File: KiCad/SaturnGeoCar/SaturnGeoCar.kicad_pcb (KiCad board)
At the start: 2 copper layers, 1 part, among them U3 ESP32-WROVER-E

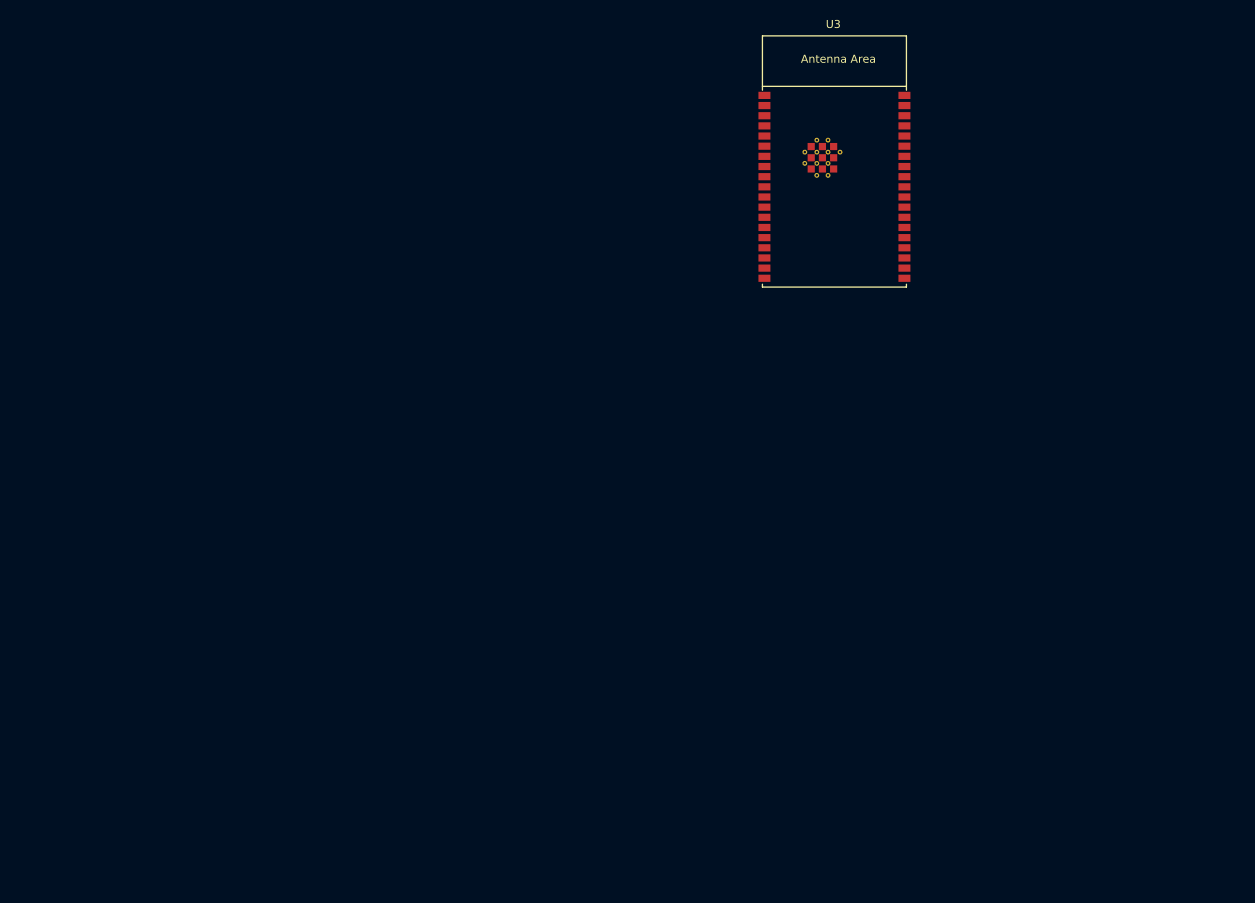
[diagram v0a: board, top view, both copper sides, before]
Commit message: Finished uploading all components, wiring has started
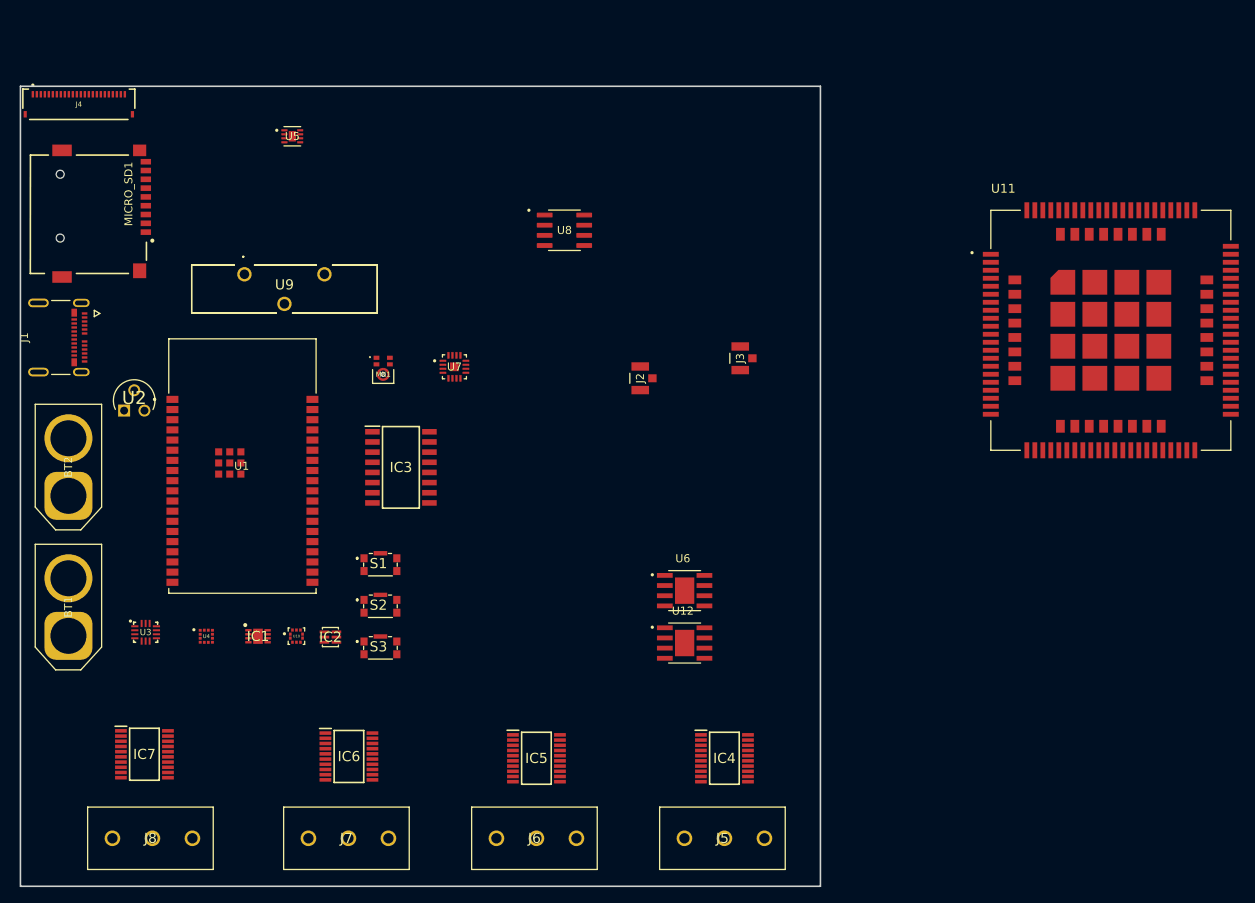
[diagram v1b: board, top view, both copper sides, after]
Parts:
- added BT1: XT60-F, Connector_AMASS:AMASS_XT60-F_1x02_P7.20mm_Vertical, F.Cu at (69.0, 139.7)
- added BT2: XT60-F, Connector_AMASS:AMASS_XT60-F_1x02_P7.20mm_Vertical, F.Cu at (69.0, 122.2)
- added IC1: SHT30-ARP-B2.5KS, SHT30-ARP-B2.5KS:SON50P250X250X100-9N-D, F.Cu at (92.7, 139.8)
- added IC2: TSL25911FN, TSL25911FN:TSL25911FN, F.Cu at (101.8, 139.8)
- added IC3: SN74HC165NSR, SN74HC165NSR:SOIC127P780X200-16N, F.Cu at (110.6, 118.6)
- added IC4: DRV8300DPWR, DRV8300DPWR:SOP65P640X120-20N, F.Cu at (151.0, 155.0)
- added IC5: DRV8300DPWR, DRV8300DPWR:SOP65P640X120-20N, F.Cu at (127.5, 155.0)
- added IC6: DRV8300DPWR, DRV8300DPWR:SOP65P640X120-20N, F.Cu at (104.1, 154.8)
- added IC7: DRV8300DPWR, DRV8300DPWR:SOP65P640X120-20N, F.Cu at (78.5, 154.5)
- added J1: 1054500101, FilesNeeded:MOLEX_1054500101, F.Cu at (63.5, 102.4)
- added J2: U.FL-R-SMT-1_80_, U.FL-R-SMT-1_80_:HIROSE_U.FL-R-SMT-1_80_, F.Cu at (140.5, 107.5)
- added J3: U.FL-R-SMT-1_80_, U.FL-R-SMT-1_80_:HIROSE_U.FL-R-SMT-1_80_, F.Cu at (153.0, 105.0)
- added J4: FFC2B28-24-G, FFC2B28-24-G:GCT_FFC2B28-24-G, F.Cu at (70.3, 73.2)
- added J5: WJ126V-5.0-3P, WJ126V-5.0-3P:WJ126V503P, F.Cu at (146.0, 165.0)
- added J6: WJ126V-5.0-3P, WJ126V-5.0-3P:WJ126V503P, F.Cu at (122.5, 165.0)
- added J7: WJ126V-5.0-3P, WJ126V-5.0-3P:WJ126V503P, F.Cu at (99.0, 165.0)
- added J8: WJ126V-5.0-3P, WJ126V-5.0-3P:WJ126V503P, F.Cu at (74.5, 165.0)
- added MICRO_SD1: TF-01A, TF-01A:TF-01A, F.Cu at (71.5, 87.0)
- added MK1: SPH0641LU4H-1, SPH0641LU4H-1:MIC_SPH0641LU4H-1, F.Cu at (108.3, 107.0)
- added S1: KMR221GLFS, KMR221GLFS:KMR231GLFS, F.Cu at (108.0, 130.8)
- added S2: KMR221GLFS, KMR221GLFS:KMR231GLFS, F.Cu at (108.0, 136.0)
- added S3: KMR221GLFS, KMR221GLFS:KMR231GLFS, F.Cu at (108.0, 141.2)
- added U1: ESP32-WROVER-E-N16R8, footprints:ESP32-WROVER-E_EXP, F.Cu at (90.8, 118.5)
- added U10: BMP388, BMP388:PQFN50P200X200X80-10N, F.Cu at (97.5, 139.7)
- added U11: SIM7600G, SIM7600G:IC_SIM7600G, F.Cu at (199.3, 101.5)
- added U12: MP1584EN-LF-Z, MP1584EN-LF-Z:SOIC127P600X170-9N, F.Cu at (146.0, 140.6)
- added U2: MCP1700-3302E_TO, MCP1700-3302E_TO:TO127P254X495-3, F.Cu at (78.5, 109.0)
- added U4: LIS3MDLTR, LIS3MDLTR:XDCR_LIS3MDLTR, F.Cu at (86.2, 139.8)
- added U5: MAX17048G_T10, MAX17048G_T10:SON50P200X200X80-9N, F.Cu at (97.0, 77.2)
- added U6: MP1584EN-LF-Z, MP1584EN-LF-Z:SOIC127P600X170-9N, F.Cu at (146.0, 134.0)
- added U7: MAX98357AETE_T, MAX98357AETE_T:QFN50P300X300X80-17N, F.Cu at (117.2, 106.1)
- added U8: PCF8563T_5_518, PCF8563T_5_518:SOIC127P599X175-8N, F.Cu at (131.0, 89.0)
- added U9: CR2032-BS-5-1, CR2032-BS-5-1:CR2032BS51, F.Cu at (91.0, 94.5)
- U3: value ESP32-WROVER-E -> LSM6DS3TR-C; footprint footprints:ESP32-WROVER-E_ThermalVias -> LSM6DS3TR-C:LGA-14-2.5X3MM
- moved U3 104.3 mm to (78.7, 139.2)
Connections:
- U3 pad 1: GND -> unconnected-(U3-SDO/SA0-Pad1)
- U3 pad 10: unconnected-(U3-DAC_1/ADC2_CH8/GPIO25-Pad10) -> (no net)
- U3 pad 11: unconnected-(U3-DAC_2/ADC2_CH9/GPIO26-Pad11) -> (no net)
- U3 pad 6: unconnected-(U3-GPIO34/ADC1_CH6-Pad6) -> GND
- U3 pad 7: unconnected-(U3-GPIO35/ADC1_CH7-Pad7) -> GND
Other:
- board outline added: 100 x 100 mm

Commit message: finshed adding all componets, everything is wired properly. Adding solar panel next
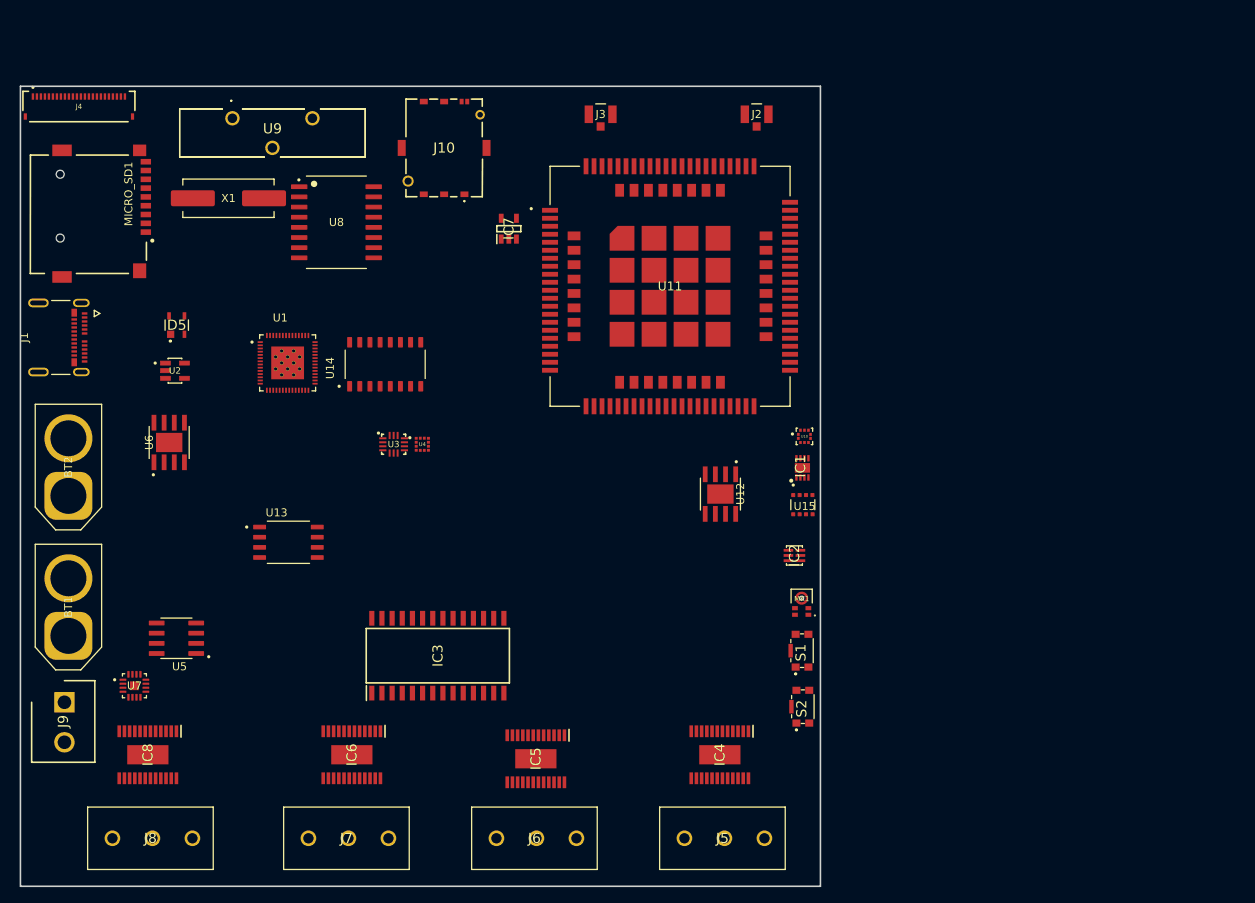
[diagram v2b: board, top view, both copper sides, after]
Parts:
- removed S3: KMR221GLFS, KMR221GLFS:KMR231GLFS
- added D5: TPD2E001DZDR, TPD2E001DZDR:TPD2E001DZDR, F.Cu at (82.5, 100.8)
- added IC8: DRV10983PWPR, DRV10983PWPR:SOP65P640X120-25N, F.Cu at (78.9, 154.6)
- added J10: SIM8055-6-1-14-01-A, SIM8055-6-1-14-01-A:SIM8055611401A, F.Cu at (116.0, 78.7)
- added J9: WJ126V-5.0-2P, WJ126V-5.0-2P:SHDR2W105P0X500_1X2_1000X780X1040P, F.Cu at (68.5, 148.0)
- added U13: W25Q128JVSIQ, W25Q128JVSIQ:SOIC127P790X216-8N, F.Cu at (96.5, 128.0)
- added U14: CH340C, CH340C:SOIC127P600X180-16N, F.Cu at (108.6, 105.8)
- added U15: BME680, BME680:PSON80P300X300X100-8N, F.Cu at (160.8, 123.3)
- added X1: X321532768KGD2SI, PCM_JLCPCB:CRYSTAL-SMD_L11.5-W4.8-LS12.7, F.Cu at (89.0, 85.0)
- IC1: value SHT30-ARP-B2.5KS -> SHT31-DIS-B2.5KS; footprint SHT30-ARP-B2.5KS:SON50P250X250X100-9N-D -> SHT31-DIS-B2.5KS:SON50P250X250X100-9N-D
- IC3: value SN74HC165NSR -> MCP23017-E_SO; footprint SN74HC165NSR:SOIC127P780X200-16N -> MCP23017-E_SO:SOIC127P1030X265-28N
- IC4, IC5, IC6: value DRV8300DPWR -> DRV10983PWPR; footprint DRV8300DPWR:SOP65P640X120-20N -> DRV10983PWPR:SOP65P640X120-25N
- IC7: value DRV8300DPWR -> AP2112K-1.8TRG1; footprint DRV8300DPWR:SOP65P640X120-20N -> AP2112K-1.8TRG1:SOT95P285X140-5N
- U1: value ESP32-WROVER-E-N16R8 -> ESP32-S3; footprint footprints:ESP32-WROVER-E_EXP -> ESP32-S3:IC_ESP32-S3
- U2: value MCP1700-3302E_TO -> AP2112K-3.3TRG1; footprint MCP1700-3302E_TO:TO127P254X495-3 -> AP2112K-3.3TRG1:SOT95P285X140-5N
- U5: value MAX17048G_T10 -> INA219AID; footprint MAX17048G_T10:SON50P200X200X80-9N -> INA219AID:SOIC127P599X175-8N
- U8: value PCF8563T_5_518 -> DS3231SN_T_R; footprint PCF8563T_5_518:SOIC127P599X175-8N -> DS3231SN_T_R:SOIC127P1032X265-16N
- moved IC7 79.9 mm to (124.0, 88.8), turned to 90 degrees
- moved IC1 71.2 mm to (160.8, 118.7), turned to 90 degrees
- moved U10 68.2 mm to (161.0, 114.8)
- moved U6 67.0 mm to (81.6, 115.5), turned to 90 degrees
- moved U5 64.4 mm to (82.5, 140.0), turned to 180 degrees
- moved MK1 59.3 mm to (160.7, 135.0), turned to 180 degrees
- moved IC2 58.9 mm to (159.8, 129.7), turned to 180 degrees
- moved U7 56.5 mm to (77.2, 145.9)
- moved U11 55.4 mm to (144.2, 96.0)
- moved S2 54.3 mm to (160.8, 148.6), turned to 90 degrees
- moved S1 53.8 mm to (160.7, 141.6), turned to 90 degrees
- moved U3 38.9 mm to (109.7, 115.8)
- moved U4 36.1 mm to (113.2, 115.8)
- moved J2 36.1 mm to (155.0, 74.5), turned to 0 degrees
- moved J3 35.1 mm to (135.5, 74.5), turned to 0 degrees
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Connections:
- IC1 pad 1: unconnected-(IC1-RH-Pad1) -> SDA
- IC1 pad 2: unconnected-(IC1-R_1-Pad2) -> GND
- IC1 pad 4: unconnected-(IC1-T-Pad4) -> SCL
- IC1 pad 5: unconnected-(IC1-VDD-Pad5) -> +3V3
- IC1 pad 6: unconnected-(IC1-NRESET-Pad6) -> +3V3
- IC1 pad 8: unconnected-(IC1-VSS-Pad8) -> GND
- IC1 pad 9: unconnected-(IC1-EP-Pad9) -> GND
- IC2 pad 1: unconnected-(IC2-SCL-Pad1) -> SCL
- IC2 pad 5: unconnected-(IC2-VDD-Pad5) -> +3V3
- IC2 pad 6: unconnected-(IC2-SDA-Pad6) -> SDA
- IC3 pad 1: unconnected-(IC3-SH/~{LD}-Pad1) -> DIR1
- IC3 pad 10: unconnected-(IC3-SER-Pad10) -> GND
- IC3 pad 12: unconnected-(IC3-B-Pad12) -> SCL
- IC3 pad 13: unconnected-(IC3-C-Pad13) -> SDA
- IC3 pad 15: unconnected-(IC3-CLK_INH-Pad15) -> GND
- IC3 pad 16: unconnected-(IC3-VCC-Pad16) -> GND
- IC3 pad 2: unconnected-(IC3-CLK-Pad2) -> DIR2
- IC3 pad 3: unconnected-(IC3-E-Pad3) -> DIR3
- IC3 pad 4: unconnected-(IC3-F-Pad4) -> DIR4
- IC3 pad 5: unconnected-(IC3-G-Pad5) -> CardDetect
- IC3 pad 9: unconnected-(IC3-QH-Pad9) -> +3V3
- IC4 pad 1: unconnected-(IC4-INHA-Pad1) -> Net-(IC4-VCP)
- IC4 pad 10: unconnected-(IC4-GLB-Pad10) -> SCL
- IC4 pad 11: unconnected-(IC4-GLA-Pad11) -> SDA
- IC4 pad 13: unconnected-(IC4-GHC-Pad13) -> SPEED1
- IC4 pad 14: unconnected-(IC4-BSTC-Pad14) -> DIR1
- IC4 pad 15: unconnected-(IC4-SHB-Pad15) -> GND
- IC4 pad 16: unconnected-(IC4-GHB-Pad16) -> GND
- IC4 pad 17: unconnected-(IC4-BSTB-Pad17) -> U1
- IC4 pad 18: unconnected-(IC4-SHA-Pad18) -> U1
- IC4 pad 19: unconnected-(IC4-GHA-Pad19) -> V1
- IC4 pad 2: unconnected-(IC4-INHB-Pad2) -> Net-(IC4-CPP)
- IC4 pad 20: unconnected-(IC4-BSTA-Pad20) -> V1
- IC4 pad 3: unconnected-(IC4-INHC-Pad3) -> Net-(IC4-CPN)
- IC4 pad 4: unconnected-(IC4-INLA-Pad4) -> Net-(IC4-SW)
- IC4 pad 5: unconnected-(IC4-INLB-Pad5) -> GND
- IC4 pad 6: unconnected-(IC4-INLC-Pad6) -> Net-(IC4-VREG)
- IC4 pad 7: unconnected-(IC4-GVDD-Pad7) -> Net-(IC4-V1P8)
- IC4 pad 8: unconnected-(IC4-GND-Pad8) -> GND
- IC4 pad 9: unconnected-(IC4-GLC-Pad9) -> Net-(IC4-V3P3)
- IC5 pad 1: unconnected-(IC5-INHA-Pad1) -> Net-(IC5-VCP)
- IC5 pad 10: unconnected-(IC5-GLB-Pad10) -> SCL
- IC5 pad 11: unconnected-(IC5-GLA-Pad11) -> SDA
- IC5 pad 13: unconnected-(IC5-GHC-Pad13) -> SPEED2
- IC5 pad 14: unconnected-(IC5-BSTC-Pad14) -> DIR2
- IC5 pad 15: unconnected-(IC5-SHB-Pad15) -> GND
- IC5 pad 16: unconnected-(IC5-GHB-Pad16) -> GND
- IC5 pad 17: unconnected-(IC5-BSTB-Pad17) -> U2
- IC5 pad 18: unconnected-(IC5-SHA-Pad18) -> U2
- IC5 pad 19: unconnected-(IC5-GHA-Pad19) -> V2
- IC5 pad 2: unconnected-(IC5-INHB-Pad2) -> Net-(IC5-CPP)
- IC5 pad 20: unconnected-(IC5-BSTA-Pad20) -> V2
- IC5 pad 3: unconnected-(IC5-INHC-Pad3) -> Net-(IC5-CPN)
- IC5 pad 4: unconnected-(IC5-INLA-Pad4) -> Net-(IC5-SW)
- IC5 pad 5: unconnected-(IC5-INLB-Pad5) -> GND
- IC5 pad 6: unconnected-(IC5-INLC-Pad6) -> Net-(IC5-VREG)
- IC5 pad 7: unconnected-(IC5-GVDD-Pad7) -> Net-(IC5-V1P8)
- IC5 pad 8: unconnected-(IC5-GND-Pad8) -> GND
- IC5 pad 9: unconnected-(IC5-GLC-Pad9) -> Net-(IC5-V3P3)
- IC6 pad 1: unconnected-(IC6-INHA-Pad1) -> Net-(IC6-VCP)
- IC6 pad 10: unconnected-(IC6-GLB-Pad10) -> SCL
- IC6 pad 11: unconnected-(IC6-GLA-Pad11) -> SDA
- IC6 pad 13: unconnected-(IC6-GHC-Pad13) -> SPEED3
- IC6 pad 14: unconnected-(IC6-BSTC-Pad14) -> DIR3
- IC6 pad 15: unconnected-(IC6-SHB-Pad15) -> GND
- IC6 pad 16: unconnected-(IC6-GHB-Pad16) -> GND
- IC6 pad 17: unconnected-(IC6-BSTB-Pad17) -> U3
- IC6 pad 18: unconnected-(IC6-SHA-Pad18) -> U3
- IC6 pad 19: unconnected-(IC6-GHA-Pad19) -> V3
- IC6 pad 2: unconnected-(IC6-INHB-Pad2) -> Net-(IC6-CPP)
- IC6 pad 20: unconnected-(IC6-BSTA-Pad20) -> V3
- IC6 pad 3: unconnected-(IC6-INHC-Pad3) -> Net-(IC6-CPN)
- IC6 pad 4: unconnected-(IC6-INLA-Pad4) -> Net-(IC6-SW)
- IC6 pad 5: unconnected-(IC6-INLB-Pad5) -> GND
- IC6 pad 6: unconnected-(IC6-INLC-Pad6) -> Net-(IC6-VREG)
- IC6 pad 7: unconnected-(IC6-GVDD-Pad7) -> Net-(IC6-V1P8)
- IC6 pad 8: unconnected-(IC6-GND-Pad8) -> GND
- IC6 pad 9: unconnected-(IC6-GLC-Pad9) -> Net-(IC6-V3P3)
- IC7 pad 1: unconnected-(IC7-INHA-Pad1) -> +5V
- IC7 pad 2: unconnected-(IC7-INHB-Pad2) -> GND
- IC7 pad 3: unconnected-(IC7-INHC-Pad3) -> +5V
- IC7 pad 5: unconnected-(IC7-INLB-Pad5) -> +1.8V
- J1 pad A4: unconnected-(J1-VBUS_A4-PadA4) -> +5V
- J1 pad A5: unconnected-(J1-CC1-PadA5) -> Net-(J1-CC1)
- J1 pad A6: unconnected-(J1-D1+-PadA6) -> D+
- J1 pad A7: unconnected-(J1-D1--PadA7) -> D-
- J1 pad A9: unconnected-(J1-VBUS_A9-PadA9) -> +5V
- J1 pad B4: unconnected-(J1-VBUS_B4-PadB4) -> +5V
- J1 pad B5: unconnected-(J1-CC2-PadB5) -> Net-(J1-CC2)
- J1 pad B6: unconnected-(J1-D2+-PadB6) -> D+
- J1 pad B7: unconnected-(J1-D2--PadB7) -> D-
- J1 pad B9: unconnected-(J1-VBUS_B9-PadB9) -> +5V
- J1 pad SH1: unconnected-(J1-SHIELD3-PadSH1) -> GND
- J1 pad SH2: unconnected-(J1-SHIELD4-PadSH2) -> GND
- J1 pad SH3: unconnected-(J1-SHIELD1-PadSH3) -> GND
- J1 pad SH4: unconnected-(J1-SHIELD2-PadSH4) -> GND
- J2 pad SIG: unconnected-(J2-PadSIG) -> LTEA
- J3 pad SIG: unconnected-(J3-PadSIG) -> GNSSA
- J4 pad 1: unconnected-(J4-Pad1) -> +3V3
- J4 pad 10: unconnected-(J4-Pad10) -> CAMXCLK
- J4 pad 11: unconnected-(J4-Pad11) -> CAMPWDN
- J4 pad 14: unconnected-(J4-Pad14) -> D0
- J4 pad 15: unconnected-(J4-Pad15) -> D1
- J4 pad 16: unconnected-(J4-Pad16) -> D2
- J4 pad 17: unconnected-(J4-Pad17) -> D3
- J4 pad 18: unconnected-(J4-Pad18) -> D4
- J4 pad 19: unconnected-(J4-Pad19) -> D5
- J4 pad 2: unconnected-(J4-Pad2) -> +3V3
- J4 pad 20: unconnected-(J4-Pad20) -> D6
- J4 pad 21: unconnected-(J4-Pad21) -> D7
- J4 pad 22: unconnected-(J4-Pad22) -> CAMPCLK
- J4 pad 23: unconnected-(J4-Pad23) -> CAMXCLK
- J4 pad 24: unconnected-(J4-Pad24) -> GND
- J4 pad 3: unconnected-(J4-Pad3) -> +3V3
- J4 pad 4: unconnected-(J4-Pad4) -> GND
- J4 pad 5: unconnected-(J4-Pad5) -> GND
- J4 pad 6: unconnected-(J4-Pad6) -> SDA
- J4 pad 7: unconnected-(J4-Pad7) -> SCL
- J4 pad 8: unconnected-(J4-Pad8) -> GND
- J4 pad 9: unconnected-(J4-Pad9) -> RESET
- J5 pad 1: unconnected-(J5-Pad1) -> U1
- J5 pad 2: unconnected-(J5-Pad2) -> V1
- J5 pad 3: unconnected-(J5-Pad3) -> W1
- J6 pad 1: unconnected-(J6-Pad1) -> U2
- J6 pad 2: unconnected-(J6-Pad2) -> V2
- J6 pad 3: unconnected-(J6-Pad3) -> W2
- J7 pad 1: unconnected-(J7-Pad1) -> U3
- J7 pad 2: unconnected-(J7-Pad2) -> V3
- J7 pad 3: unconnected-(J7-Pad3) -> W3
- J8 pad 1: unconnected-(J8-Pad1) -> U4
- J8 pad 2: unconnected-(J8-Pad2) -> V4
- J8 pad 3: unconnected-(J8-Pad3) -> W4
- MICRO_SD1 pad 2: unconnected-(MICRO_SD1-CD/DAT3-Pad2) -> SDDAT3
- MICRO_SD1 pad 3: unconnected-(MICRO_SD1-CMD-Pad3) -> SDCMD
- MICRO_SD1 pad 4: unconnected-(MICRO_SD1-VDD-Pad4) -> +3V3
- MICRO_SD1 pad 5: unconnected-(MICRO_SD1-CLK-Pad5) -> SDCLK
- MICRO_SD1 pad 6: unconnected-(MICRO_SD1-VSS-Pad6) -> GND
- MICRO_SD1 pad 7: unconnected-(MICRO_SD1-DAT0-Pad7) -> SDDAT0
- MICRO_SD1 pad CD1: unconnected-(MICRO_SD1-CD-PadCD1) -> CardDetect
- MK1 pad 1: unconnected-(MK1-DATA-Pad1) -> DATA
- MK1 pad 2: unconnected-(MK1-SELECT-Pad2) -> GND
- MK1 pad 4: unconnected-(MK1-CLOCK-Pad4) -> BCLK
- MK1 pad 5: unconnected-(MK1-VDD-Pad5) -> +3V3
- S1 pad 1: unconnected-(S1-COM_1-Pad1) -> RESET
- S1 pad 2: unconnected-(S1-NO_1-Pad2) -> GND
- S1 pad 5: unconnected-(S1-GND-Pad5) -> GND
- U1 pad 1: GND -> unconnected-(U1-LNA_IN-Pad1)
- U1 pad 10: unconnected-(U1-IO25-Pad10) -> SDA
- U1 pad 11: unconnected-(U1-IO26-Pad11) -> BCLK
- U1 pad 12: unconnected-(U1-IO27-Pad12) -> LRCLK
- U1 pad 13: unconnected-(U1-IO14-Pad13) -> DIN
- U1 pad 14: unconnected-(U1-IO12-Pad14) -> PWRKEY
- U1 pad 15: GND -> SPEED4
- U1 pad 16: unconnected-(U1-IO13-Pad16) -> SPEED3
- U1 pad 17: unconnected-(U1-NC_2-Pad17) -> SPEED2
- U1 pad 18: unconnected-(U1-NC_3-Pad18) -> SPEED1
- U1 pad 19: unconnected-(U1-NC_4-Pad19) -> SDCMD
- U1 pad 2: unconnected-(U1-3V3-Pad2) -> +3V3
- U1 pad 20: unconnected-(U1-NC_5-Pad20) -> +3V3
- U1 pad 21: unconnected-(U1-NC_6-Pad21) -> Net-(U1-XTAL_32K_P)
- U1 pad 22: unconnected-(U1-NC_7-Pad22) -> Net-(U1-XTAL_32K_N)
- U1 pad 23: unconnected-(U1-IO15-Pad23) -> SDDAT0
- U1 pad 24: unconnected-(U1-IO2-Pad24) -> SDCLK
- U1 pad 25: unconnected-(U1-IO0-Pad25) -> SDDAT3
- U1 pad 26: unconnected-(U1-IO4-Pad26) -> D-
- U1 pad 27: unconnected-(U1-NC_8-Pad27) -> D+
- U1 pad 29: unconnected-(U1-IO5-Pad29) -> +3V3
- U1 pad 3: unconnected-(U1-EN-Pad3) -> +3V3
- U1 pad 30: unconnected-(U1-IO18-Pad30) -> FIO3
- U1 pad 31: unconnected-(U1-IO19-Pad31) -> FIO2
- U1 pad 32: unconnected-(U1-NC-Pad32) -> FCS
- U1 pad 33: unconnected-(U1-IO21-Pad33) -> FCLK
- U1 pad 34: unconnected-(U1-RXD0-Pad34) -> FIO0
- U1 pad 35: unconnected-(U1-TXD0-Pad35) -> FIO1
- U1 pad 37: unconnected-(U1-IO23-Pad37) -> FCLK
- U1 pad 38: GND -> D4
- U1 pad 39: GND -> D1
- U1 pad 4: unconnected-(U1-SENSOR_VP-Pad4) -> RESET
- U1 pad 40: GND -> D2
- U1 pad 41: GND -> D3
- U1 pad 42: GND -> unconnected-(U1-GPIO37-Pad42)
- U1 pad 43: GND -> RESET
- U1 pad 44: GND -> CAMXCLK
- U1 pad 45: GND -> CAMPCLK
- U1 pad 46: GND -> +3V3
- U1 pad 47: GND -> D7
- U1 pad 5: unconnected-(U1-SENSOR_VN-Pad5) -> D5
- U1 pad 6: unconnected-(U1-IO34-Pad6) -> uC_TX
- U1 pad 7: unconnected-(U1-IO35-Pad7) -> uC_RX
- U1 pad 8: unconnected-(U1-IO32-Pad8) -> CAMPWDN
- U1 pad 9: unconnected-(U1-IO33-Pad9) -> SCL
- U10 pad 1: unconnected-(U10-VDDIO-Pad1) -> +3V3
- U10 pad 10: unconnected-(U10-VDD-Pad10) -> +3V3
- U10 pad 2: unconnected-(U10-SCK-Pad2) -> SCL
- U10 pad 3: Net-(U10-VSS-Pad3) -> GND
- U10 pad 4: unconnected-(U10-SDI-Pad4) -> SDA
- U10 pad 5: unconnected-(U10-SDO-Pad5) -> GND
- U10 pad 6: unconnected-(U10-CSB-Pad6) -> +3V3
- U10 pad 8: Net-(U10-VSS-Pad3) -> GND
- U10 pad 9: Net-(U10-VSS-Pad3) -> GND
- U11 pad 1: Net-(U11A-GND-Pad1) -> GND
- U11 pad 10: Net-(U11A-GND-Pad1) -> GND
- U11 pad 100: Net-(U11B-RESERVED-Pad100) -> unconnected-(U11B-RESERVED-Pad100)_4
- U11 pad 101: Net-(U11B-RESERVED-Pad100) -> unconnected-(U11B-RESERVED-Pad100)_10
- U11 pad 102: Net-(U11B-RESERVED-Pad100) -> unconnected-(U11B-RESERVED-Pad100)_7
- U11 pad 103: Net-(U11B-RESERVED-Pad100) -> unconnected-(U11B-RESERVED-Pad100)
- U11 pad 104: Net-(U11B-RESERVED-Pad100) -> unconnected-(U11B-RESERVED-Pad100)_8
- U11 pad 105: Net-(U11B-RESERVED-Pad100) -> unconnected-(U11B-RESERVED-Pad100)_6
- U11 pad 11: unconnected-(U11A-USB_VBUS-Pad11) -> +5V
- U11 pad 110: Net-(U11A-GND-Pad1) -> GND
- U11 pad 111: Net-(U11B-RESERVED-Pad100) -> unconnected-(U11B-RESERVED-Pad100)_5
- U11 pad 118: Net-(U11A-GND-Pad1) -> GND
- U11 pad 12: unconnected-(U11A-USB_DN-Pad12) -> D-
- U11 pad 120: Net-(U11A-GND-Pad1) -> GND
- U11 pad 121: Net-(U11A-GND-Pad1) -> GND
- U11 pad 122: Net-(U11A-GND-Pad1) -> GND
- U11 pad 123: Net-(U11A-GND-Pad1) -> GND
- U11 pad 124: Net-(U11A-GND-Pad1) -> GND
- U11 pad 125: Net-(U11A-GND-Pad1) -> GND
- U11 pad 126: Net-(U11A-GND-Pad1) -> GND
- U11 pad 127: Net-(U11A-GND-Pad1) -> GND
- U11 pad 128: Net-(U11A-GND-Pad1) -> GND
- U11 pad 129: Net-(U11A-GND-Pad1) -> GND
- U11 pad 13: unconnected-(U11A-USB_DP-Pad13) -> D+
- U11 pad 130: Net-(U11A-GND-Pad1) -> GND
- U11 pad 131: Net-(U11A-GND-Pad1) -> GND
- U11 pad 132: Net-(U11A-GND-Pad1) -> GND
- U11 pad 133: Net-(U11A-GND-Pad1) -> GND
- U11 pad 134: Net-(U11A-GND-Pad1) -> GND
- U11 pad 135: Net-(U11A-GND-Pad1) -> GND
- U11 pad 14: Net-(U11A-GND-Pad1) -> GND
- U11 pad 17: unconnected-(U11A-USIM_DATA-Pad17) -> SIMDATA
- U11 pad 18: unconnected-(U11A-USIM_RST-Pad18) -> SIMRESET
- U11 pad 19: unconnected-(U11A-USIM_CLK-Pad19) -> SIMCLK
- U11 pad 2: Net-(U11A-GND-Pad1) -> GND
- U11 pad 20: unconnected-(U11A-USIM_VDD-Pad20) -> SIMVCC
- U11 pad 3: unconnected-(U11A-~{PWRKEY}-Pad3) -> PWRKEY
- U11 pad 37: Net-(U11A-GND-Pad1) -> GND
- U11 pad 4: unconnected-(U11A-~{RESET}-Pad4) -> RESET
- U11 pad 40: Net-(U11A-GND-Pad1) -> GND
- U11 pad 41: Net-(U11A-GND-Pad1) -> GND
- U11 pad 43: Net-(U11A-GND-Pad1) -> GND
- U11 pad 5: Net-(U11A-GND-Pad1) -> GND
- U11 pad 53: unconnected-(U11A-USIM_DET-Pad53) -> SIMCD
- U11 pad 54: unconnected-(U11A-FLIGHTMODE-Pad54) -> Net-(U11A-FLIGHTMODE)
- U11 pad 55: unconnected-(U11A-SCL-Pad55) -> SCL
- U11 pad 56: unconnected-(U11A-SDA-Pad56) -> SDA
- U11 pad 57: Net-(U11A-GND-Pad1) -> GND
- U11 pad 58: Net-(U11A-GND-Pad1) -> GND
- U11 pad 60: Net-(U11A-GND-Pad1) -> GND
- U11 pad 61: Net-(U11A-GND-Pad1) -> GND
- U11 pad 64: Net-(U11A-GND-Pad1) -> GND
- U11 pad 65: Net-(U11A-GND-Pad1) -> GND
- U11 pad 68: unconnected-(U11A-RXD-Pad68) -> uC_RX
- U11 pad 71: unconnected-(U11A-TXD-Pad71) -> uC_TX
- U11 pad 77: Net-(U11A-GND-Pad1) -> GND
- U11 pad 78: Net-(U11A-GND-Pad1) -> GND
- U11 pad 79: unconnected-(U11A-GNSS_ANT-Pad79) -> GNSSA
- U11 pad 80: Net-(U11A-GND-Pad1) -> GND
- U11 pad 81: Net-(U11A-GND-Pad1) -> GND
- U11 pad 82: unconnected-(U11A-MAIN_ANT-Pad82) -> LTEA
- U11 pad 83: unconnected-(U11A-COEX1-Pad83) -> GND
- U11 pad 84: unconnected-(U11A-COEX2-Pad84) -> GND
- U11 pad 86: unconnected-(U11A-COEX3-Pad86) -> GND
- U11 pad 88: Net-(U11B-RESERVED-Pad100) -> unconnected-(U11B-RESERVED-Pad100)_3
- U11 pad 89: Net-(U11B-RESERVED-Pad100) -> unconnected-(U11B-RESERVED-Pad100)_11
- U11 pad 90: Net-(U11B-RESERVED-Pad100) -> unconnected-(U11B-RESERVED-Pad100)_2
- U11 pad 91: Net-(U11B-RESERVED-Pad100) -> unconnected-(U11B-RESERVED-Pad100)_9
- U11 pad 92: Net-(U11B-RESERVED-Pad100) -> unconnected-(U11B-RESERVED-Pad100)_1
- U11 pad 93: Net-(U11A-GND-Pad1) -> GND
- U11 pad 98: Net-(U11A-GND-Pad1) -> GND
- U11 pad 99: Net-(U11B-RESERVED-Pad100) -> unconnected-(U11B-RESERVED-Pad100)_12
- U12 pad 1: unconnected-(U12-SW-Pad1) -> Net-(D2-K)
- U12 pad 2: unconnected-(U12-EN-Pad2) -> Net-(U12-EN)
- U12 pad 3: unconnected-(U12-COMP-Pad3) -> Net-(U12-COMP)
- U12 pad 4: unconnected-(U12-FB-Pad4) -> Net-(U12-FB)
- U12 pad 5: unconnected-(U12-GND-Pad5) -> GND
- U12 pad 6: unconnected-(U12-FREQ-Pad6) -> Net-(U12-FREQ)
- U12 pad 7: unconnected-(U12-VIN-Pad7) -> +11.1V
- U12 pad 8: unconnected-(U12-BST-Pad8) -> Net-(U12-BST)
- U12 pad 9: unconnected-(U12-EP-Pad9) -> GND
- U2 pad 1: GND -> +5V
- U2 pad 2: unconnected-(U2-VIN-Pad2) -> GND
- U2 pad 3: unconnected-(U2-VOUT-Pad3) -> +5V
- U3 pad 1: unconnected-(U3-SDO/SA0-Pad1) -> GND
- U3 pad 12: unconnected-(U3-CS-Pad12) -> +3V3
- U3 pad 13: unconnected-(U3-SCL-Pad13) -> SCL
- U3 pad 14: unconnected-(U3-SDA-Pad14) -> SDA
- U3 pad 5: unconnected-(U3-VDDIO-Pad5) -> +3V3
- U3 pad 8: unconnected-(U3-VDD-Pad8) -> +3V3
- U4 pad 1: unconnected-(U4-SCL/SPC-Pad1) -> SCL
- U4 pad 10: unconnected-(U4-CS-Pad10) -> +3V3
- U4 pad 11: unconnected-(U4-SDA/SDI/SDO-Pad11) -> SDA
- U4 pad 12: unconnected-(U4-RSVD2-Pad12) -> GND
- U4 pad 2: unconnected-(U4-RSVD1-Pad2) -> GND
- U4 pad 4: unconnected-(U4-C1-Pad4) -> Net-(U4-C1)
- U4 pad 5: unconnected-(U4-VDD-Pad5) -> +3V3
- U4 pad 6: unconnected-(U4-VDD_IO-Pad6) -> +3V3
- U4 pad 9: unconnected-(U4-SDO/SA1-Pad9) -> GND
- U5 pad 1: unconnected-(U5-CTG-Pad1) -> GND
- U5 pad 2: unconnected-(U5-CELL-Pad2) -> GND
- U5 pad 3: unconnected-(U5-VDD-Pad3) -> SDA
- U5 pad 4: GND -> SCL
- U5 pad 5: unconnected-(U5-~{ALERT}-Pad5) -> +3V3
- U5 pad 6: unconnected-(U5-QSTRT-Pad6) -> GND
- U5 pad 7: unconnected-(U5-SCL-Pad7) -> +11.1V
- U5 pad 8: unconnected-(U5-SDA-Pad8) -> GND
- U6 pad 1: unconnected-(U6-SW-Pad1) -> Net-(D1-K)
- U6 pad 2: unconnected-(U6-EN-Pad2) -> Net-(U6-EN)
- U6 pad 3: unconnected-(U6-COMP-Pad3) -> Net-(U6-COMP)
- U6 pad 4: unconnected-(U6-FB-Pad4) -> Net-(U6-FB)
- U6 pad 5: unconnected-(U6-GND-Pad5) -> GND
- U6 pad 6: unconnected-(U6-FREQ-Pad6) -> Net-(U6-FREQ)
- U6 pad 7: unconnected-(U6-VIN-Pad7) -> +11.1V
- U6 pad 8: unconnected-(U6-BST-Pad8) -> Net-(U6-BST)
- U6 pad 9: unconnected-(U6-EP-Pad9) -> GND
- U8 pad 2: unconnected-(U8-0SCO-Pad2) -> +3V3
- U8 pad 5: unconnected-(U8-SDA-Pad5) -> (no net)
- U8 pad 6: unconnected-(U8-SCL-Pad6) -> (no net)
- U8 pad 7: unconnected-(U8-CLKOUT-Pad7) -> (no net)
- U8 pad 8: unconnected-(U8-VDD-Pad8) -> (no net)
- U9 pad 1: unconnected-(U9-+_1-Pad1) -> Net-(U8-VBAT)
- U9 pad 2: unconnected-(U9-+_2-Pad2) -> Net-(U8-VBAT)
- U9 pad 3: unconnected-(U9---Pad3) -> GND

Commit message: hehe easyeda sucks (almost done)
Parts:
- added Y1: X322540MPB4SI, X322540MPB4SI:X322540MPB4SI, F.Cu at (94.4, 101.2)
- moved X1 47.6 mm to (109.5, 128.0)
- moved U1 8.56 mm to (95.4, 114.1)
- moved U7 1.80 mm to (78.8, 146.9)
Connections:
- IC3 pad 25: unconnected-(IC3-GPA4-Pad25) -> LED4
- IC3 pad 26: unconnected-(IC3-GPA5-Pad26) -> LED3
- IC3 pad 27: unconnected-(IC3-GPA6-Pad27) -> LED2
- IC3 pad 28: unconnected-(IC3-GPA7-Pad28) -> LED1
- IC3 pad 6: unconnected-(IC3-GPB5-Pad6) -> COM1
- S2 pad 1: unconnected-(S2-COM_1-Pad1) -> COM1
- S2 pad 2: unconnected-(S2-NO_1-Pad2) -> GND
- S2 pad 5: unconnected-(S2-GND-Pad5) -> GND
- U1 pad 53: unconnected-(U1-XTAL_N-Pad53) -> Net-(U1-XTAL_N)
- U1 pad 54: unconnected-(U1-XTAL_P-Pad54) -> Net-(U1-XTAL_P)
- U11 pad 51: unconnected-(U11A-NETLIGHT-Pad51) -> NETLIGHT
- U7 pad 1: unconnected-(U7-DIN-Pad1) -> DIN
- U7 pad 10: unconnected-(U7-OUTN-Pad10) -> NS
- U7 pad 14: unconnected-(U7-LRCLK-Pad14) -> LRCLK
- U7 pad 16: unconnected-(U7-BCLK-Pad16) -> BCLK
- U7 pad 17: unconnected-(U7-EP-Pad17) -> GND
- U7 pad 2: unconnected-(U7-GAIN_SLOT-Pad2) -> GND
- U7 pad 4: unconnected-(U7-SD_MODE-Pad4) -> GND
- U7 pad 7: Net-(U7-VDD-Pad7) -> +3V3
- U7 pad 8: Net-(U7-VDD-Pad7) -> +3V3
- U7 pad 9: unconnected-(U7-OUTP-Pad9) -> PS
- X1 pad 1: Net-(U8-X1) -> Net-(U1-XTAL_32K_P)
- X1 pad 2: Net-(U8-X2) -> Net-(U1-XTAL_32K_N)
